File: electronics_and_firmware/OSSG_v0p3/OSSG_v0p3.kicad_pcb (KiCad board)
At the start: 2 copper layers, 85 x 9 mm, 0 parts

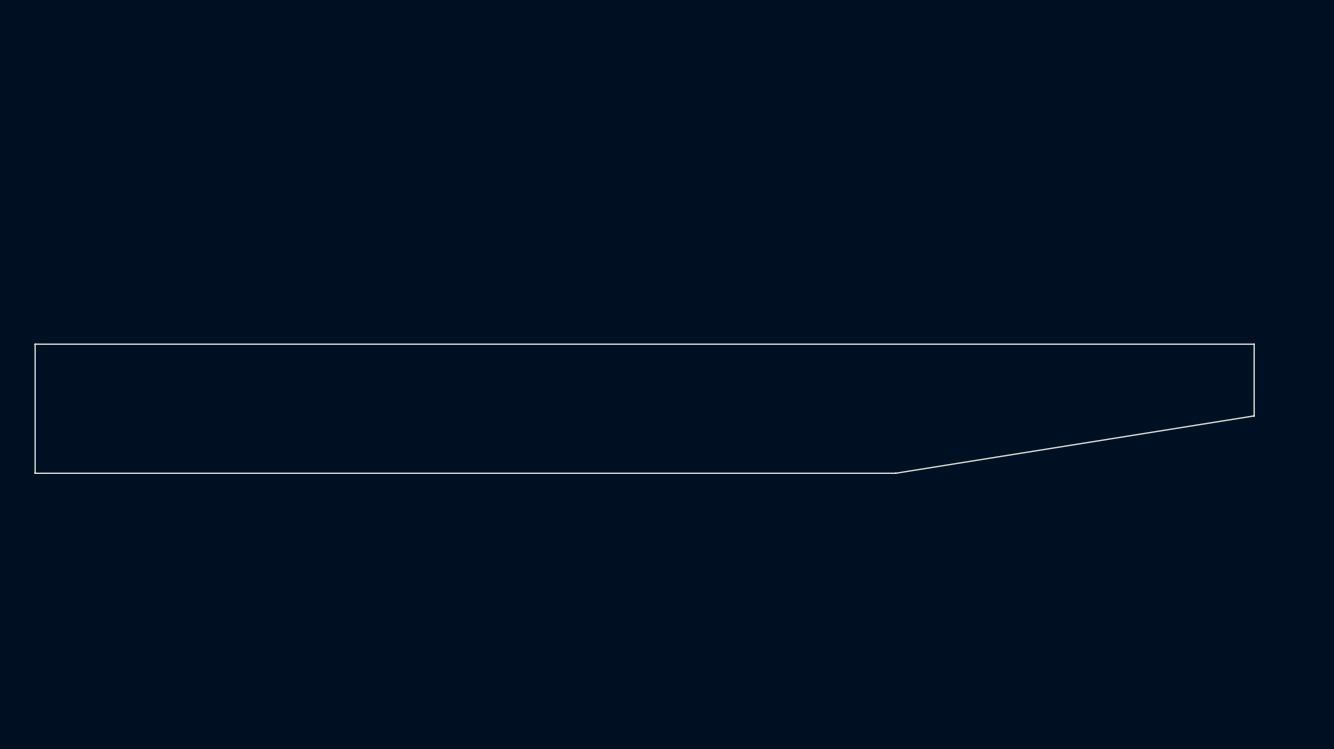
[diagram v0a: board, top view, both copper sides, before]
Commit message: start PCB layout, small schematic fixes
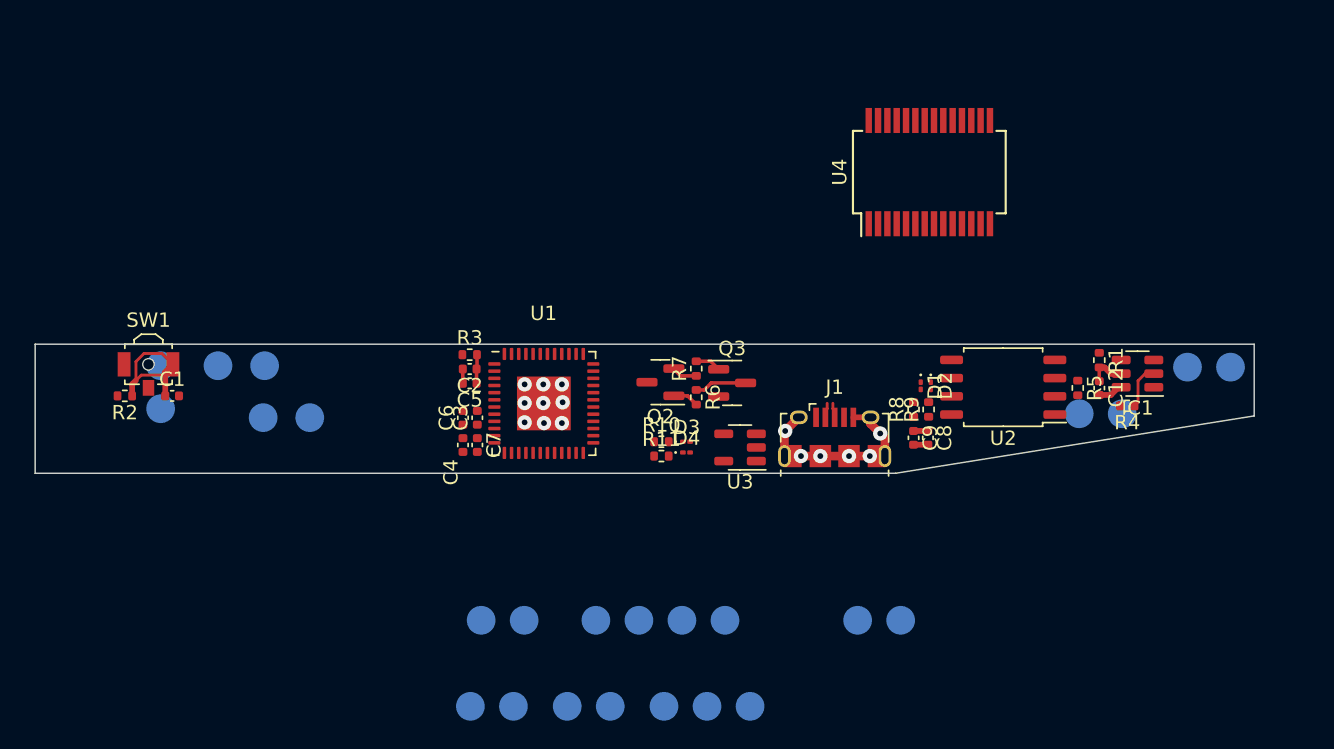
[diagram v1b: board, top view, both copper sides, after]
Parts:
- added C1: 1uF, Capacitor_SMD:C_0402_1005Metric, F.Cu at (84.6, 78.6)
- added C12: 100nF, Capacitor_SMD:C_0402_1005Metric, F.Cu at (149.2, 78.1)
- added C2: 10uF, Capacitor_SMD:C_0402_1005Metric, F.Cu at (105.3, 76.7)
- added C3: 0.1uF, Capacitor_SMD:C_0402_1005Metric, F.Cu at (105.8, 80.1)
- added C4: 0.1uF, Capacitor_SMD:C_0402_1005Metric, F.Cu at (104.8, 82.0)
- added C5: 0.1uF, Capacitor_SMD:C_0402_1005Metric, F.Cu at (105.3, 77.7)
- added C6: 0.1uF, Capacitor_SMD:C_0402_1005Metric, F.Cu at (104.8, 80.1)
- added C7: 0.1uF, Capacitor_SMD:C_0402_1005Metric, F.Cu at (105.8, 82.0)
- added C8: 4.7uF, Capacitor_SMD:C_0402_1005Metric, F.Cu at (137.2, 81.5)
- added C9: 10nF, Capacitor_SMD:C_0402_1005Metric, F.Cu at (136.2, 81.5)
- added D1: LED, Diode_SMD:D_01005_0402Metric, F.Cu at (136.8, 77.9)
- added D2: LED, Diode_SMD:D_01005_0402Metric, F.Cu at (137.4, 77.9)
- added D3: RX, Diode_SMD:D_01005_0402Metric, F.Cu at (120.4, 81.8)
- added D4: TX, Diode_SMD:D_01005_0402Metric, F.Cu at (120.4, 82.5)
- added IC1: DW01A, Package_TO_SOT_SMD:SOT-23-6, F.Cu at (151.9, 77.0)
- added J1: USB_B_Micro, Connector_USB:USB_Micro-B_Amphenol_10118194_Horizontal, F.Cu at (130.8, 81.5)
- added Q2: Q_NPN_BEC, Package_TO_SOT_SMD:SOT-23, F.Cu at (118.6, 77.7)
- added Q3: Q_NPN_BEC, Package_TO_SOT_SMD:SOT-23, F.Cu at (123.6, 77.7)
- added R1: 100, Resistor_SMD:R_0402_1005Metric, F.Cu at (149.2, 76.1)
- added R10: 270R, Resistor_SMD:R_0402_1005Metric, F.Cu at (118.7, 81.8)
- added R11: 270R, Resistor_SMD:R_0402_1005Metric, F.Cu at (118.7, 82.8)
- added R2: 10k, Resistor_SMD:R_0402_1005Metric, F.Cu at (81.3, 78.6)
- added R3: 0R, Resistor_SMD:R_0402_1005Metric, F.Cu at (105.3, 75.7)
- added R4: 1K, Resistor_SMD:R_0402_1005Metric, F.Cu at (151.2, 79.3)
- added R5: 4K, Resistor_SMD:R_0402_1005Metric, F.Cu at (147.7, 78.0)
- added R6: 10K, Resistor_SMD:R_0402_1005Metric, F.Cu at (121.1, 78.7)
- added R7: 10K, Resistor_SMD:R_0402_1005Metric, F.Cu at (121.1, 76.7)
- added R8: 330R, Resistor_SMD:R_0402_1005Metric, F.Cu at (136.2, 79.5)
- added R9: 330R, Resistor_SMD:R_0402_1005Metric, F.Cu at (137.3, 79.5)
- added SW1: SW_SPST, Button_Switch_SMD:SW_SPST_B3U-3100P-B, F.Cu at (82.9, 77.2)
- added TP1: IO4_Touch0, OpenSourceSmartGlasses:BreakoutPadSmall, B.Cu at (118.8, 100.2)
- added TP10: IO37_ADC1C0, OpenSourceSmartGlasses:BreakoutPadSmall, B.Cu at (87.8, 76.5)
- added TP11: IO38_ADC1C1, OpenSourceSmartGlasses:BreakoutPadSmall, B.Cu at (91.0, 76.5)
- added TP12: IO39_ADC1C3, OpenSourceSmartGlasses:BreakoutPadSmall, B.Cu at (94.2, 80.1)
- added TP13: L_Pos_Battery_Terminal, OpenSourceSmartGlasses:BreakoutPadSmall, B.Cu at (155.3, 76.6)
- added TP14: L_Neg_Battery_Terminal, OpenSourceSmartGlasses:BreakoutPadSmall, B.Cu at (147.8, 79.8)
- added TP15: R_Pos_Battery_Terminal, OpenSourceSmartGlasses:BreakoutPadSmall, B.Cu at (158.3, 76.6)
- added TP16: R_Neg_Battery_Terminal, OpenSourceSmartGlasses:BreakoutPadSmall, B.Cu at (150.8, 79.8)
- added TP17: +3.3V_Breakout, OpenSourceSmartGlasses:BreakoutPadSmall, B.Cu at (83.8, 76.5)
- added TP18: GND_Breakout, OpenSourceSmartGlasses:BreakoutPadSmall, B.Cu at (83.8, 79.5)
- added TP19: IO15_SPI2_CS, OpenSourceSmartGlasses:BreakoutPadSmall, B.Cu at (114.1, 94.2)
- added TP2: IO36_ADC1C2, OpenSourceSmartGlasses:BreakoutPadSmall, B.Cu at (90.9, 80.1)
- added TP20: IO15_SPI2_SCLK, OpenSourceSmartGlasses:BreakoutPadSmall, B.Cu at (117.1, 94.2)
- added TP21: IO15_SPI2_MOSI, OpenSourceSmartGlasses:BreakoutPadSmall, B.Cu at (120.1, 94.2)
- added TP22: IO15_SPI2_MISO, OpenSourceSmartGlasses:BreakoutPadSmall, B.Cu at (123.1, 94.2)
- added TP23: IO0_Breakout, OpenSourceSmartGlasses:BreakoutPadSmall, B.Cu at (124.8, 100.2)
- added TP24: IO17_U2TXD, OpenSourceSmartGlasses:BreakoutPadSmall, B.Cu at (132.3, 94.2)
- added TP25: IO16_U2RXD, OpenSourceSmartGlasses:BreakoutPadSmall, B.Cu at (135.3, 94.2)
- added TP3: RXIN, OpenSourceSmartGlasses:BreakoutPadSmall, B.Cu at (105.3, 100.2)
- added TP4: TXIN, OpenSourceSmartGlasses:BreakoutPadSmall, B.Cu at (108.3, 100.2)
- added TP5: IO2_Touch2, OpenSourceSmartGlasses:BreakoutPadSmall, B.Cu at (121.8, 100.2)
- added TP6: IO25_DAC1, OpenSourceSmartGlasses:BreakoutPadSmall, B.Cu at (106.1, 94.2)
- added TP7: IO26_DAC2, OpenSourceSmartGlasses:BreakoutPadSmall, B.Cu at (109.1, 94.2)
- added TP8: IO21_I2C_SDA0, OpenSourceSmartGlasses:BreakoutPadSmall, B.Cu at (112.1, 100.2)
- added TP9: IO22_I2C_SCL0, OpenSourceSmartGlasses:BreakoutPadSmall, B.Cu at (115.1, 100.2)
- added U1: ESP32-PICO-D4, OpenSourceSmartGlasses:ESP32_PICO_D4_smallGND, F.Cu at (110.5, 79.1)
- added U2: TP4056, Package_SO:SOP-8_5.28x5.23mm_P1.27mm, F.Cu at (142.5, 78.0)
- added U3: XC6222B331MRG, Package_TO_SOT_SMD:SOT-23-5, F.Cu at (124.2, 82.2)
- added U4: FT232RL, Package_SO:SSOP-28_5.3x10.2mm_P0.65mm, F.Cu at (137.3, 63.0)
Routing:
- net GND: track 0.00 -> 15.5 mm, vias 0 -> 15
- net EN: track 0.00 -> 10.3 mm
- net DTR: track 0.00 -> 3.64 mm
- net Net-(IC1-Pad2): track 0.00 -> 3.16 mm
- net Net-(C12-Pad1): track 0.00 -> 2.66 mm
- net +3.3VA: track 0.00 -> 2.01 mm
- net Net-(Q2-Pad1): track 0.00 -> 1.82 mm
- net RTS: track 0.00 -> 1.80 mm
- net Net-(Q3-Pad1): track 0.00 -> 1.79 mm
- net BATT-: track 0.00 -> 1.75 mm
- net VCC_IN: track 0.00 -> 1.06 mm
- net USB_-: track 0.00 -> 1.03 mm
- net USB_+: track 0.00 -> 1.03 mm
- added copper zone on In2.Cu, net +3V3
- added copper zone on In1.Cu, net GND
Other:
- copper layers 2 -> 4

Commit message: battery voltage divider, fix USB GND, add USB reverse voltage diode, update footprints of everything, update layout
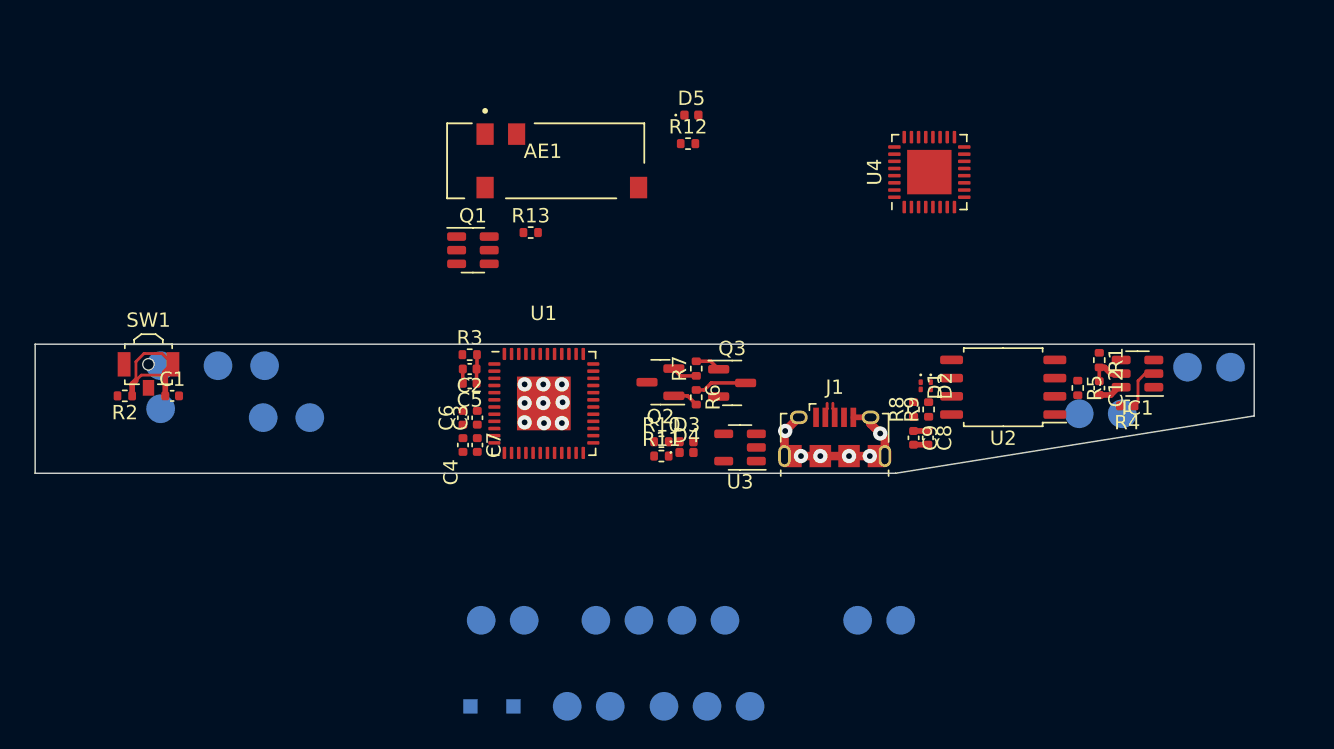
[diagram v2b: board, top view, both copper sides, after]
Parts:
- added AE1: PRO-OB-440, OpenSourceSmartGlasses:PRO_OB_440_antenna, F.Cu at (110.4, 62.0)
- added D5: D_Schottky, Diode_SMD:D_0402_1005Metric, F.Cu at (120.8, 59.0)
- added Q1: FS8205A, Package_TO_SOT_SMD:SOT-23-6, F.Cu at (105.5, 68.4)
- added R12: 442K, Resistor_SMD:R_0402_1005Metric, F.Cu at (120.5, 61.0)
- added R13: 160K, Resistor_SMD:R_0402_1005Metric, F.Cu at (109.6, 67.2)
- D3: value RX -> TX; footprint Diode_SMD:D_01005_0402Metric -> Diode_SMD:D_0402_1005Metric
- D4: value TX -> RX; footprint Diode_SMD:D_01005_0402Metric -> Diode_SMD:D_0402_1005Metric
- R2: value 10k -> 10K
- TP3: value RXIN -> TXIN; footprint OpenSourceSmartGlasses:BreakoutPadSmall -> TestPoint:TestPoint_Pad_1.0x1.0mm
- TP4: value TXIN -> RXIN; footprint OpenSourceSmartGlasses:BreakoutPadSmall -> TestPoint:TestPoint_Pad_1.0x1.0mm
- U4: value FT232RL -> FT232RQ; footprint Package_SO:SSOP-28_5.3x10.2mm_P0.65mm -> Package_DFN_QFN:QFN-32-1EP_5x5mm_P0.5mm_EP3.1x3.1mm
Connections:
- J1 pad 1: VCC_IN -> Net-(D5-Pad2)
- J1 pad 2: USB_- -> Net-(J1-Pad2)
- J1 pad 3: USB_+ -> Net-(J1-Pad3)
- R2 pad 2: +3.3VA -> +3V3
- TP3 pad 1: TXD -> RXD
- TP4 pad 1: RXD -> TXD
- U4 pad 1: RXD -> VCCIO
- U4 pad 11: CTS -> unconnected-(U4-Pad11)
- U4 pad 12: unconnected-(U4-Pad12) -> (no net)
- U4 pad 13: unconnected-(U4-Pad13) -> (no net)
- U4 pad 14: unconnected-(U4-Pad14) -> Net-(J1-Pad3)
- U4 pad 15: USB_+ -> Net-(J1-Pad2)
- U4 pad 16: USB_- -> VCCIO
- U4 pad 17: VCCIO -> GND
- U4 pad 18: GND -> unconnected-(U4-Pad18)
- U4 pad 2: DTR -> RXD
- U4 pad 20: VCC_IN -> GND
- U4 pad 21: GND -> Net-(R11-Pad1)
- U4 pad 22: Net-(R11-Pad1) -> Net-(R10-Pad1)
- U4 pad 23: Net-(R10-Pad1) -> (no net)
- U4 pad 24: (no net) -> GND
- U4 pad 25: GND -> (no net)
- U4 pad 3: RTS -> unconnected-(U4-Pad3)
- U4 pad 4: VCCIO -> GND
- U4 pad 5: TXD -> (no net)
- U4 pad 7: GND -> unconnected-(U4-Pad7)
- U4 pad 8: (no net) -> CTS
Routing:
- net USB_-: track 1.03 -> 0.00 mm
- net USB_+: track 1.03 -> 0.00 mm
- net Net-(J1-Pad3): track 0.00 -> 1.03 mm
- net Net-(J1-Pad2): track 0.00 -> 1.03 mm

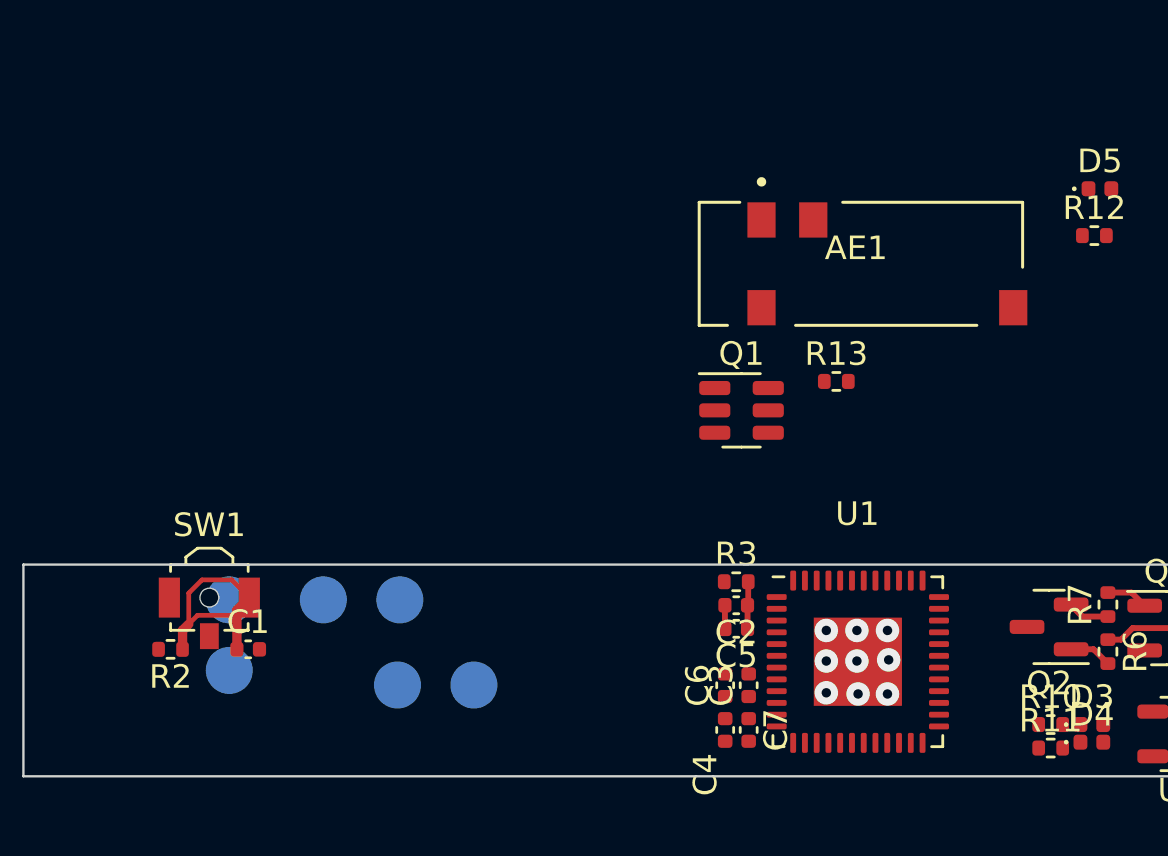
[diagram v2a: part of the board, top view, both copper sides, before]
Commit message: Changed antenna
Added keepout zone as graphic and required trace.
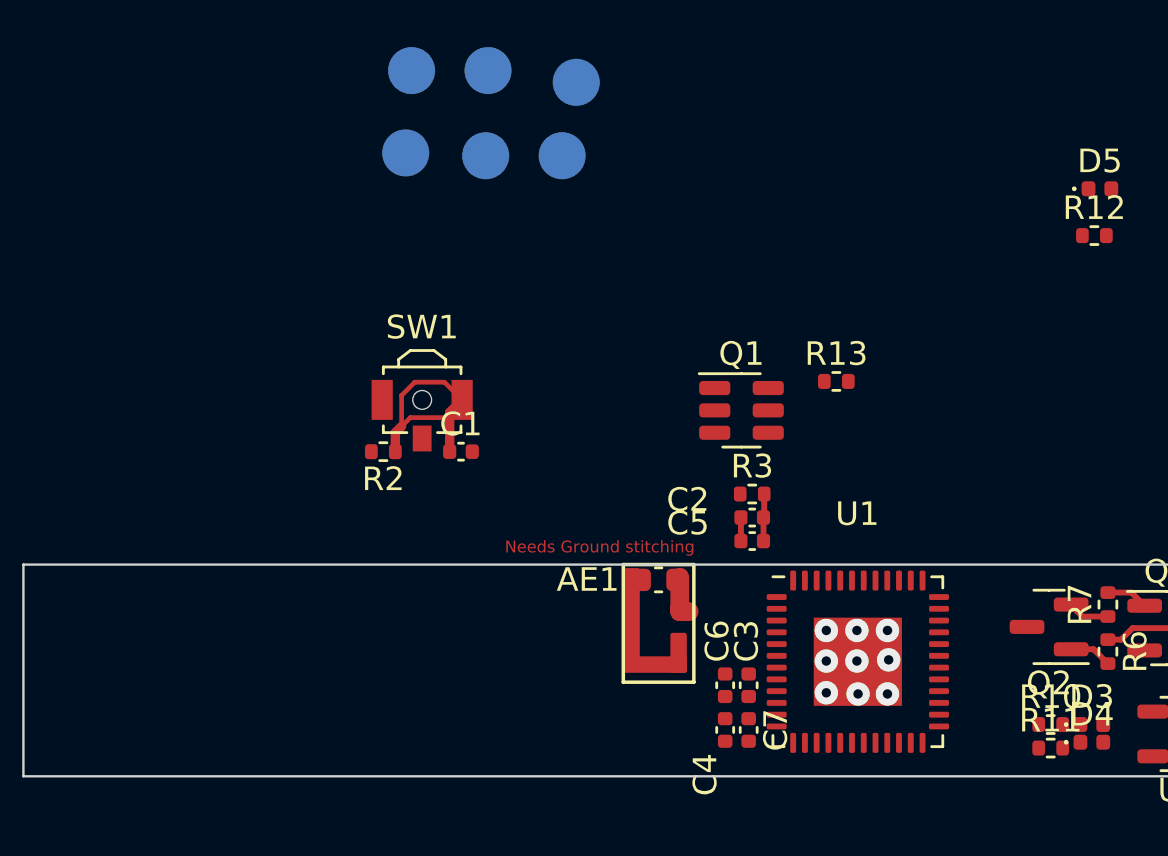
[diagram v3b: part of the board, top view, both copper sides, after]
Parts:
- AE1: value PRO-OB-440 -> 2450AT14A0100T; footprint OpenSourceSmartGlasses:PRO_OB_440_antenna -> Capacitor_SMD:C_0603_1608Metric
- moved TP17 26.5 mm to (98.5, 54.5)
- moved TP18 23.2 mm to (91.2, 57.5)
- moved TP12 22.8 mm to (97.9, 57.6)
- moved TP2 22.8 mm to (94.7, 57.6)
- moved TP10 22.8 mm to (91.5, 54.0)
- moved TP11 22.8 mm to (94.8, 54.0)
- moved AE1 16.0 mm to (102.0, 75.7), turned to 180 degrees
- moved SW1 12.3 mm to (92.0, 68.8)
- moved C1 12.3 mm to (93.6, 70.2)
- moved R2 12.3 mm to (90.3, 70.2)
- moved C2 3.79 mm to (106.0, 73.0)
- moved C5 3.79 mm to (106.0, 74.0)
- moved R3 3.79 mm to (106.0, 72.0)
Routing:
- net Net-(AE1-Pad1): track 0.00 -> 1.86 mm
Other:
- board text added: "Needs Ground stitching"
